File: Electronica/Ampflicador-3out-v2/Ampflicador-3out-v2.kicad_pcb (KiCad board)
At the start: 2 copper layers, 38 parts, among them Q1 MPF102, SW1 SW_DPST_x2, U1 LM386

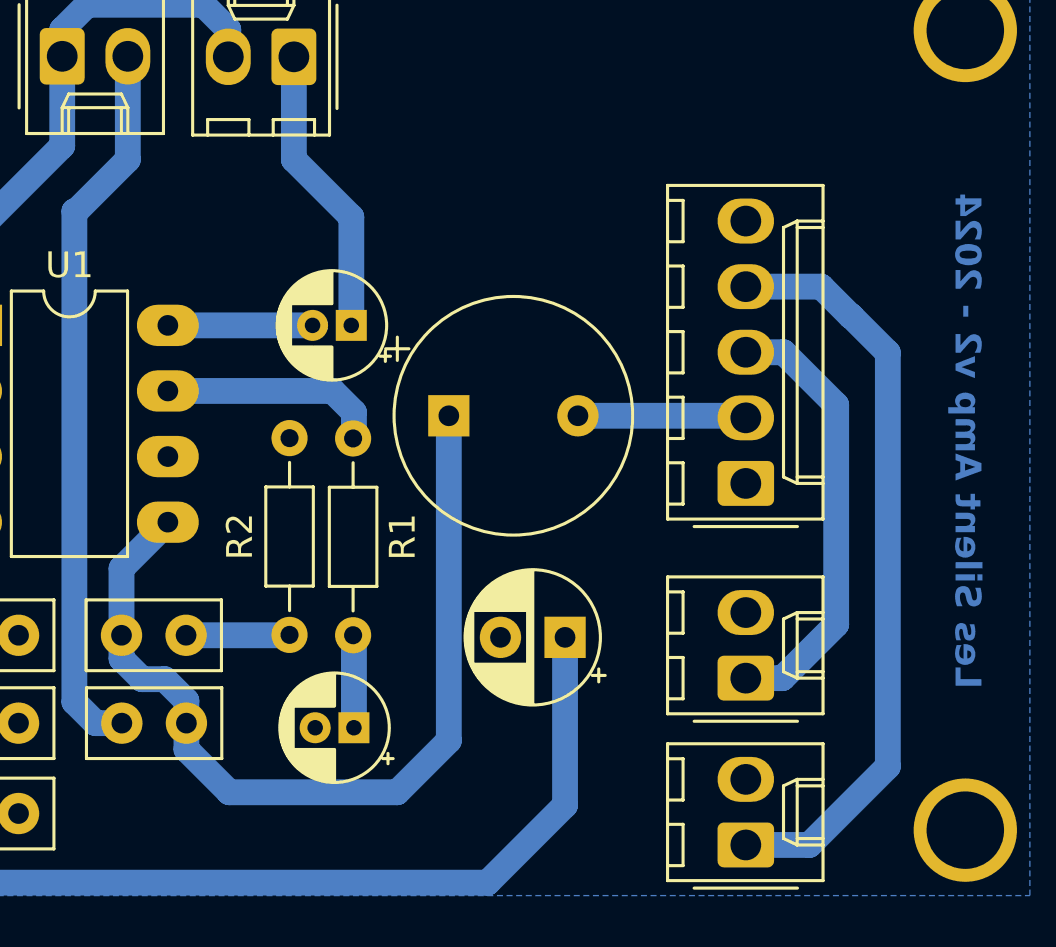
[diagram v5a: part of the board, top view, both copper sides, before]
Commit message: Amp v2 terminada - Pistas 45°
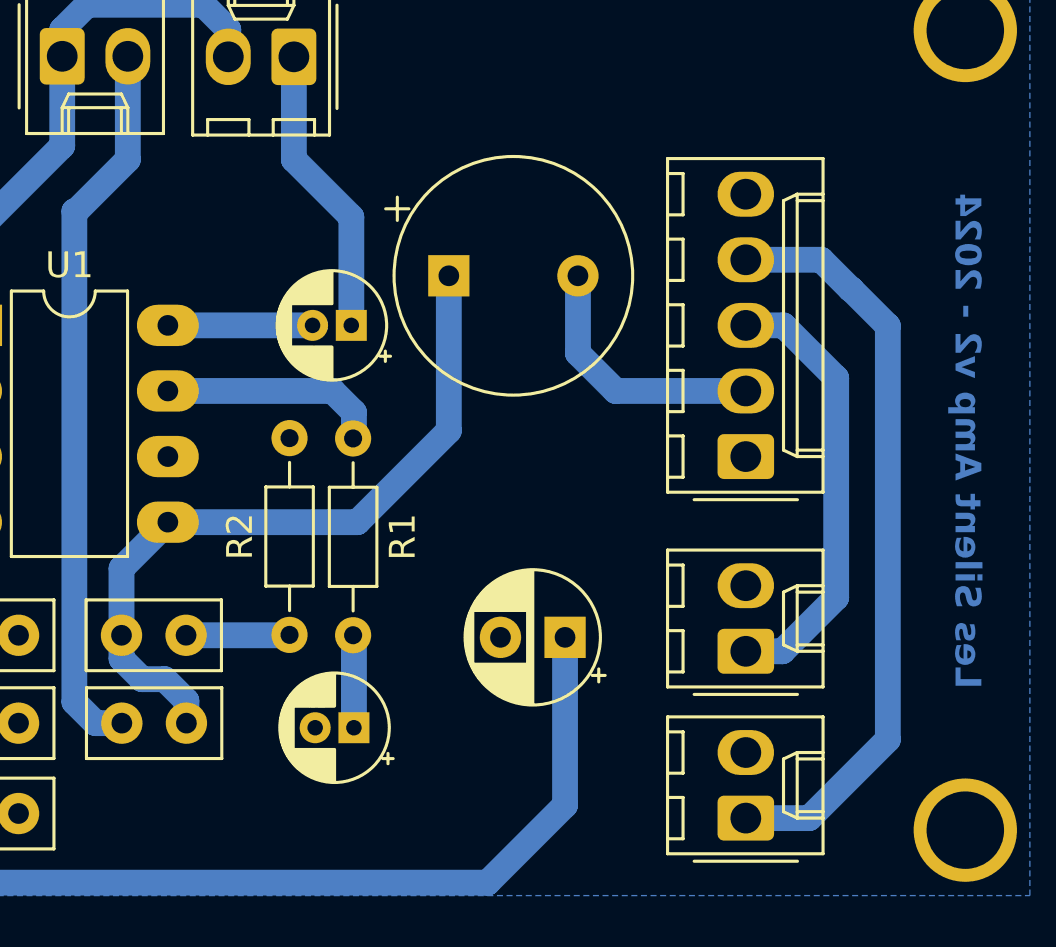
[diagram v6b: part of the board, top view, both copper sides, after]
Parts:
- moved C9 5.42 mm to (77.5, 37.5)
- moved Output-Jack-3.1 1.04 mm to (89.0, 44.5)
- moved Output-Jack-6.1 1.04 mm to (89.0, 58.5)
- moved Output-Speaker1 1.04 mm to (89.0, 52.0)
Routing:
- net Net-(C7-Pad1): track 35.4 -> 28.4 mm
- net Net-(C9-Pad2): track 6.65 -> 10.3 mm
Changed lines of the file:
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@@
 	(footprint "Connector_Molex:Molex_KK-254_AE-6410-02A_1x02_P2.54mm_Vertical"
 		(layer "F.Cu")
-		(at 89 59.54 90)
+		(at 89 58.5 90)
 		(descr "Molex KK-254 Interconnect System, old/engineering part number: AE-6410-02A example for new part number: 22-27-2021, 2 Pins (http://www.molex.com/pdm_docs/sd/022272021_sd.pdf), generated with kicad-footprint-generator")
 		(tags "connector Molex KK-254 vertical")
@@
 	(footprint "Connector_Molex:Molex_KK-254_AE-6410-05A_1x05_P2.54mm_Vertical"
 		(layer "F.Cu")
-		(at 89 45.54 90)
+		(at 89 44.5 90)
 		(descr "Molex KK-254 Interconnect System, old/engineering part number: AE-6410-05A example for new part number: 22-27-2051, 5 Pins (http://www.molex.com/pdm_docs/sd/022272021_sd.pdf), generated with kicad-footprint-generator")
 		(tags "connector Molex KK-254 vertical")
@@
 	(footprint "Capacitor_THT:CP_Radial_Tantal_D9.0mm_P5.00mm"
 		(layer "F.Cu")
-		(at 77.5 42.92)
+		(at 77.5 37.5)
 		(descr "CP, Radial_Tantal series, Radial, pin pitch=5.00mm, , diameter=9.0mm, Tantal Electrolytic Capacitor, http://cdn-reichelt.de/documents/datenblatt/B300/TANTAL-TB-Serie%23.pdf")
 		(tags "CP Radial_Tantal series Radial pin pitch 5.00mm  diameter 9.0mm Tantal Electrolytic Capacitor")
@@
 	(footprint "Connector_Molex:Molex_KK-254_AE-6410-02A_1x02_P2.54mm_Vertical"
 		(layer "F.Cu")
-		(at 89 53.08 90)
+		(at 89 52.04 90)
 		(descr "Molex KK-254 Interconnect System, old/engineering part number: AE-6410-02A example for new part number: 22-27-2021, 2 Pins (http://www.molex.com/pdm_docs/sd/022272021_sd.pdf), generated with kicad-footprint-generator")
 		(tags "connector Molex KK-254 vertical")
@@
 	)
 	(segment
-		(start 67.338578 55.838578)
-		(end 67.338578 54.822545)
+		(start 77.5 43.5)
+		(end 77.5 37.5)
 		(width 1)
 		(layer "B.Cu")
@@
 	)
 	(segment
-		(start 77.5 55.5)
-		(end 75.5 57.5)
+		(start 66.62 47.04)
+		(end 73.96 47.04)
 		(width 1)
 		(layer "B.Cu")
@@
 	)
 	(segment
-		(start 77.5 42.92)
-		(end 77.5 55.5)
+		(start 73.96 47.04)
+		(end 77.5 43.5)
 		(width 1)
 		(layer "B.Cu")
@@
 	)
 	(segment
-		(start 69 57.5)
-		(end 67.338578 55.838578)
+		(start 64.825 48.835)
+		(end 66.62 47.04)
 		(width 1)
 		(layer "B.Cu")
@@
 	)
 	(segment
-		(start 75.5 57.5)
-		(end 69 57.5)
+		(start 64.825 51.42)
+		(end 64.825 48.835)
 		(width 1)
 		(layer "B.Cu")
@@
 	)
 	(segment
-		(start 64.825 48.835)
-		(end 66.62 47.04)
+		(start 83.96 41.96)
+		(end 89 41.96)
 		(width 1)
 		(layer "B.Cu")
-		(net 9)
+		(net 10)
 	)
 	(segment
-		(start 64.825 51.42)
-		(end 64.825 48.835)
+		(start 82.5 37.5)
+		(end 82.5 40.5)
 		(width 1)
 		(layer "B.Cu")
-		(net 9)
+		(net 10)
 	)
 	(segment
-		(start 88.92 42.92)
-		(end 89 43)
+		(start 88.917817 41.877817)
+		(end 89 41.96)
 		(width 1)
 		(layer "B.Cu")
@@
 	)
 	(segment
-		(start 88.917817 42.917817)
-		(end 89 43)
+		(start 82.5 40.5)
+		(end 83.96 41.96)
 		(width 1)
 		(layer "B.Cu")
@@
 	)
 	(segment
-		(start 82.5 42.92)
-		(end 88.92 42.92)
+		(start 88.92 41.88)
+		(end 89 41.96)
 		(width 1)
 		(layer "B.Cu")
@@
 	)
 	(segment
-		(start 92.5 51)
-		(end 92.5 42.5)
+		(start 92.5 49.96)
+		(end 92.5 41.46)
 		(width 1)
 		(layer "B.Cu")
@@
 	)
 	(segment
-		(start 92.5 42.5)
-		(end 90.46 40.46)
+		(start 92.5 41.46)
+		(end 90.46 39.42)
 		(width 1)
 		(layer "B.Cu")
@@
 	)
 	(segment
-		(start 89 53.08)
-		(end 90.42 53.08)
+		(start 89 52.04)
+		(end 90.42 52.04)
 		(width 1)
 		(layer "B.Cu")
@@
 	)
 	(segment
-		(start 90.42 53.08)
-		(end 92.5 51)
+		(start 90.42 52.04)
+		(end 92.5 49.96)
 		(width 1)
 		(layer "B.Cu")
@@
 	)
 	(segment
-		(start 90.46 40.46)
-		(end 89 40.46)
+		(start 90.46 39.42)
+		(end 89 39.42)
 		(width 1)
 		(layer "B.Cu")
@@
 	)
 	(segment
-		(start 89 59.54)
-		(end 91.46 59.54)
+		(start 89 58.5)
+		(end 91.46 58.5)
 		(width 1)
 		(layer "B.Cu")
@@
 	)
 	(segment
-		(start 94.5 40.480101)
-		(end 93.079899 39.06)
+		(start 94.5 39.440101)
+		(end 93.079899 38.02)
 		(width 1)
 		(layer "B.Cu")
@@
 	)
 	(segment
-		(start 93.06 39.06)
-		(end 91.92 37.92)
+		(start 93.06 38.02)
+		(end 91.92 36.88)
 		(width 1)
 		(layer "B.Cu")
@@
 	)
 	(segment
-		(start 91.92 37.92)
-		(end 89 37.92)
+		(start 91.92 36.88)
+		(end 89 36.88)
 		(width 1)
 		(layer "B.Cu")
@@
 	)
 	(segment
-		(start 93.079899 39.06)
-		(end 93.06 39.06)
+		(start 93.079899 38.02)
+		(end 93.06 38.02)
 		(width 1)
 		(layer "B.Cu")
@@
 	)
 	(segment
-		(start 94.5 56.5)
-		(end 94.5 40.480101)
+		(start 94.5 55.46)
+		(end 94.5 39.440101)
 		(width 1)
 		(layer "B.Cu")
@@
 	)
 	(segment
-		(start 91.46 59.54)
-		(end 94.5 56.5)
+		(start 91.46 58.5)
+		(end 94.5 55.46)
 		(width 1)
 		(layer "B.Cu")

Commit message: Amp v2 sin plano masa
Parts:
- removed R7, R8, R9: 100Ω, Resistor_THT:R_Axial_DIN0204_L3.6mm_D1.6mm_P7.62mm_Horizontal
- added SW2: SW_DPST_x2, Button_Switch_THT:SW_Slide_SPDT_Straight_CK_OS102011MS2Q, F.Cu at (39.0, 28.8)
- moved Output-Jack-3.1 6.92 mm to (89.0, 37.6)
- moved Output-Speaker1 4.25 mm to (89.0, 47.8)
- moved C6 4.00 mm to (72.5, 35.6)
- moved C9 2.55 mm to (78.0, 35.0)
- moved Q1 2.04 mm to (49.8, 56.2), turned to 180 degrees
- moved C5 1.55 mm to (72.3, 55.4)
- moved Output-Jack-6.1 1.46 mm to (89.0, 57.0)
- moved C1 1.43 mm to (57.6, 50.2)
- moved C7 1.22 mm to (64.8, 50.2)
- moved U1 1.22 mm to (59.0, 38.2)
- moved C3 0.97 mm to (60.1, 54.2)
- moved C4 0.79 mm to (57.5, 58.3)
- moved R1 0.64 mm to (74.0, 43.2)
- moved C8 0.62 mm to (64.8, 54.2)
- moved R2 0.60 mm to (71.2, 50.8)
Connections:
- C10 pad 1: Net-(C10-Pad1) -> Net-(Input1-Pin_2)
- Input1 pad 1: GND -> Net-(Input1-Pin_1)
- Input2 pad 1: GND -> Net-(Input2-Pin_1)
- Input2 pad 2: Net-(Input2-Pin_2) -> Net-(Input1-Pin_1)
- Input3 pad 2: Net-(Input3-Pin_2) -> Net-(Input2-Pin_1)
- Output-Jack-3.1 pad 5: GND -> (no net)
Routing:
- net GND: track 0.00 -> 366.2 mm
- net Net-(Input2-Pin_1): track 0.00 -> 19.6 mm
- net Net-(Input1-Pin_1): track 0.00 -> 14.0 mm
- net Net-(Input1-Pin_2): track 5.69 -> 18.0 mm
- net Net-(C7-Pad1): track 28.4 -> 39.7 mm
- net Net-(C10-Pad1): track 9.69 -> 0.00 mm
- net Net-(Input3-Pin_2): track 7.50 -> 0.00 mm
- net Net-(Input2-Pin_2): track 7.45 -> 0.00 mm
- net Net-(Output-Jack-6.1-Pin_1): track 29.3 -> 36.4 mm
- net Net-(SW1A-B): track 92.5 -> 99.5 mm
- net Net-(Output-Speaker1-Pin_1): track 17.2 -> 23.2 mm
- net Net-(C9-Pad2): track 10.3 -> 6.02 mm
- net Net-(Gain1-Pin_1): track 11.3 -> 7.02 mm
- net Net-(C11-Pad1): track 20.1 -> 23.1 mm
- net Net-(Q1-D): track 11.4 -> 14.2 mm
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- removed copper zone on B.Cu, net GND

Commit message: Amp v2 sin acordate
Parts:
- removed Gain1, Output-Jack-6.1, Power-Input1: Screw_Terminal_01x02, Connector_Molex:Molex_KK-254_AE-6410-02A_1x02_P2.54mm_Vertical
- added BT1: Power Input, Connector_Molex:Molex_KK-254_AE-6410-02A_1x02_P2.54mm_Vertical, F.Cu at (29.5, 51.1)
- added LS1: Speaker, Connector_Molex:Molex_KK-254_AE-6410-02A_1x02_P2.54mm_Vertical, F.Cu at (112.7, 35.0)
- added P1: Piezo 1, Connector_Molex:Molex_KK-254_AE-6410-02A_1x02_P2.54mm_Vertical, F.Cu at (119.8, 35.0)
- added P2: Piezo 2, Connector_Molex:Molex_KK-254_AE-6410-02A_1x02_P2.54mm_Vertical, F.Cu at (112.7, 42.9)
- added P3: Piezo 2, Connector_Molex:Molex_KK-254_AE-6410-02A_1x02_P2.54mm_Vertical, F.Cu at (119.8, 42.9)
- added RV1: Volume, Connector_Molex:Molex_KK-254_AE-6410-03A_1x03_P2.54mm_Vertical, F.Cu at (126.9, 27.1)
- added RV2: Gain, Connector_Molex:Molex_KK-254_AE-6410-02A_1x02_P2.54mm_Vertical, F.Cu at (71.6, 29.0)
- added RV3: Bass, Connector_Molex:Molex_KK-254_AE-6410-02A_1x02_P2.54mm_Vertical, F.Cu at (119.8, 50.7)
- added SW3: SW_SPDT, Connector_Molex:Molex_KK-254_AE-6410-03A_1x03_P2.54mm_Vertical, F.Cu at (126.9, 35.0)
- renumbered Output-Jack-3.1 to Output-Jack-3.5
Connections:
- C10 pad 1: Net-(Input1-Pin_2) -> Net-(C10-Pad1)
- C12 pad 2: Net-(Vol1-Pin_1) -> Net-(C12-Pad2)
- C8 pad 1: Net-(Bass1-Pin_2) -> Net-(C8-Pad1)
- Output-Jack-3.5 pad 1: GND -> (no net)
- Output-Jack-3.5 pad 2: Net-(C9-Pad2) -> (no net)
- Output-Jack-3.5 pad 3: Net-(Output-Speaker1-Pin_1) -> (no net)
- Output-Jack-3.5 pad 4: Net-(Output-Jack-6.1-Pin_1) -> (no net)
- SW2 pad 1: Net-(Input1-Pin_1) -> Net-(SW2A-A)
- U1 pad 1: Net-(Bass1-Pin_1) -> Net-(RV2-Pad2)
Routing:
- net Net-(Output-Jack-6.1-Pin_1): track 36.4 -> 0.00 mm
- net Net-(Output-Speaker1-Pin_1): track 23.2 -> 0.00 mm
- added copper zone on B.Cu, net GND
